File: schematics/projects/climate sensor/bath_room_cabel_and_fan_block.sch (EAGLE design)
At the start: 5 parts

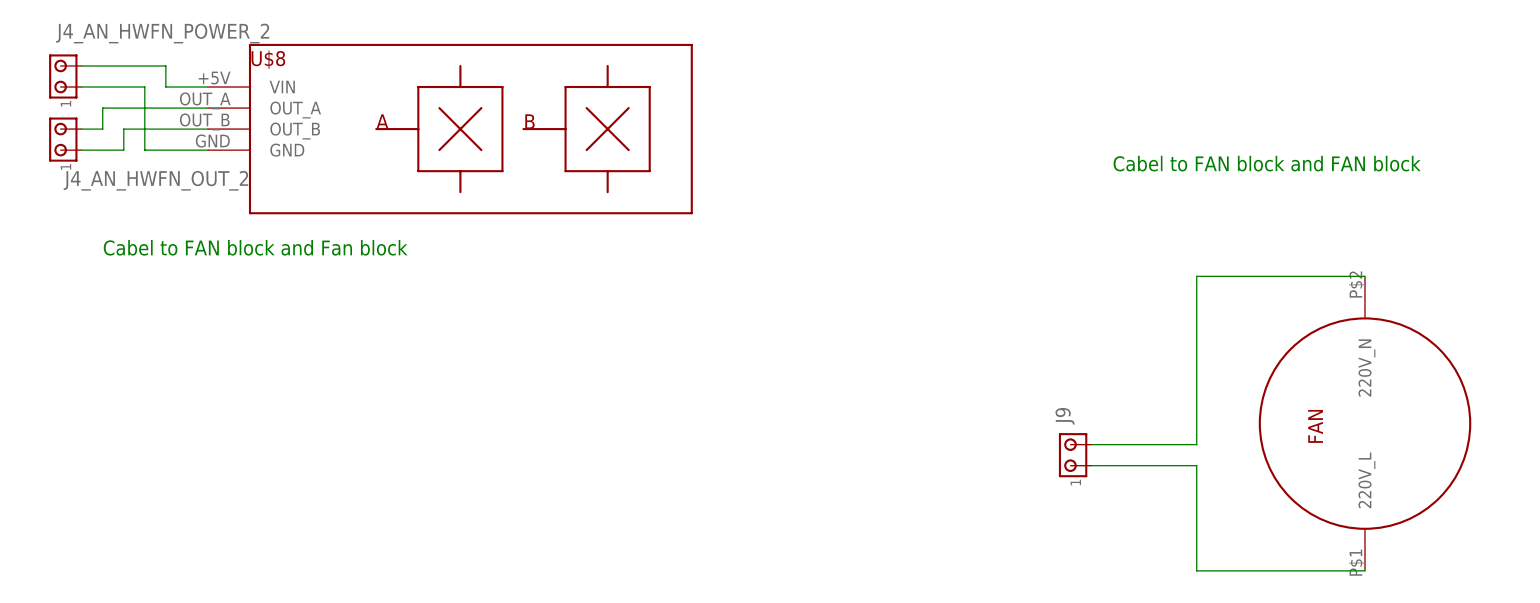
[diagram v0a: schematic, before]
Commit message: added eagle board files for low-voltage schemas
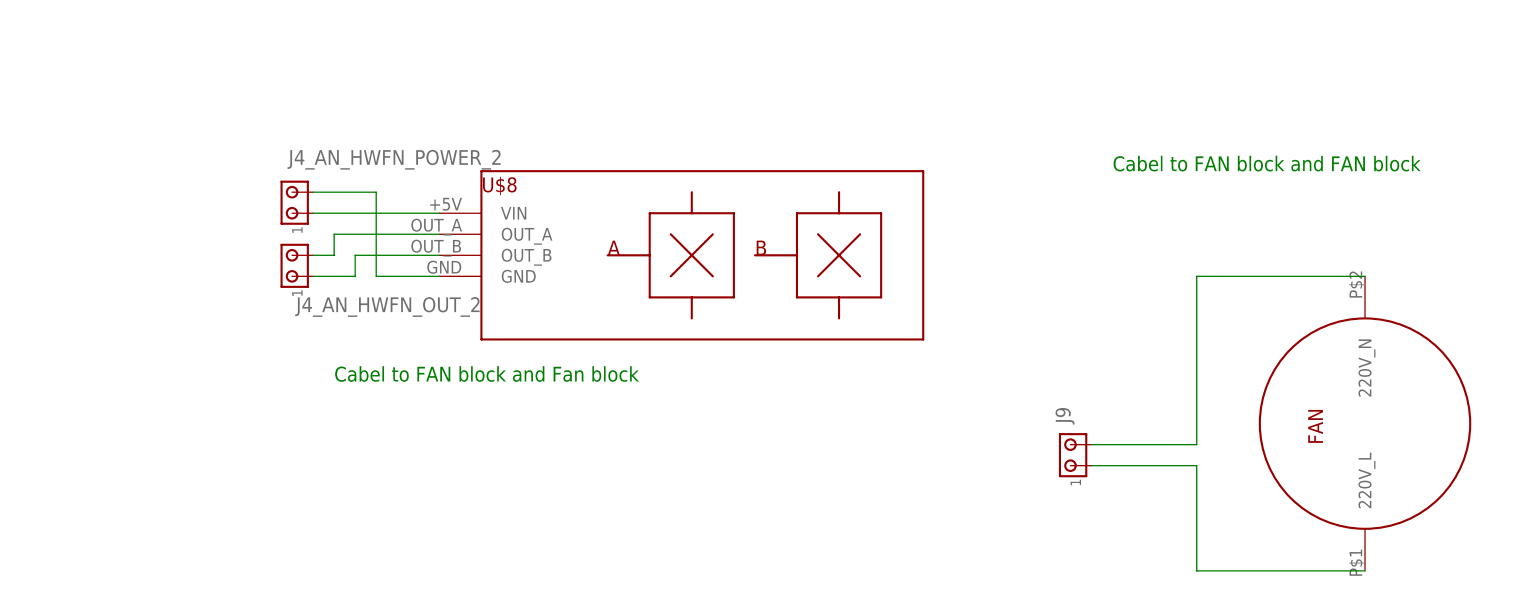
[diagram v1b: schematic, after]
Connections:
- net GND: now also J4_AN_HWFN_POWER_2.2; no longer J4_AN_HWFN_POWER_2.1
- net N$12: now also J4_AN_HWFN_POWER_2.1; no longer J4_AN_HWFN_POWER_2.2
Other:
- moved on the sheet: J4_AN_HWFN_OUT_2, J4_AN_HWFN_POWER_2, U$8
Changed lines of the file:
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@@
 </classes>
 <groups>
+<schematic_group name="FAN1"/>
 <schematic_group name="ANEMOMETER1"/>
-<schematic_group name="FAN1"/>
 </groups>
 <parts>
+<part name="U$10" library="my_devices" deviceset="FAN" device=""/>
+<part name="J9" library="con-amp" library_urn="urn:adsk.eagle:library:127" deviceset="MTA02-100" device="" package3d_urn="urn:adsk.eagle:package:8081649/1"/>
 <part name="U$8" library="my_devices" deviceset="ANEMOMETER" device=""/>
 <part name="J4_AN_HWFN_POWER_2" library="con-amp" library_urn="urn:adsk.eagle:library:127" deviceset="MTA02-100" device="" package3d_urn="urn:adsk.eagle:package:8081649/1"/>
 <part name="J4_AN_HWFN_OUT_2" library="con-amp" library_urn="urn:adsk.eagle:library:127" deviceset="MTA02-100" device="" package3d_urn="urn:adsk.eagle:package:8081649/1"/>
-<part name="U$10" library="my_devices" deviceset="FAN" device=""/>
-<part name="J9" library="con-amp" library_urn="urn:adsk.eagle:library:127" deviceset="MTA02-100" device="" package3d_urn="urn:adsk.eagle:package:8081649/1"/>
 </parts>
 <sheets>
 <sheet>
 <plain>
-<text x="-86.36" y="73.66" size="1.778" layer="91" grouprefs="ANEMOMETER1">Cabel to FAN block and Fan block</text>
 <text x="35.56" y="83.82" size="1.778" layer="91" grouprefs="FAN1">Cabel to FAN block and FAN block</text>
+<text x="-58.42" y="58.42" size="1.778" layer="91" grouprefs="ANEMOMETER1">Cabel to FAN block and Fan block</text>
 </plain>
 <instances>
-<instance part="U$8" gate="G$1" x="-53.34" y="88.9" smashed="yes" grouprefs="ANEMOMETER1">
-<attribute name="NAME" x="-68.58" y="96.52" size="1.778" layer="94"/>
-</instance>
-<instance part="J4_AN_HWFN_POWER_2" gate="G$1" x="-91.44" y="93.98" smashed="yes" rot="R90" grouprefs="ANEMOMETER1">
-<attribute name="NAME" x="-66.04" y="101.6" size="1.778" layer="95" rot="R180"/>
-<attribute name="VALUE" x="-87.63" y="99.06" size="1.778" layer="96" rot="R90"/>
-</instance>
-<instance part="J4_AN_HWFN_OUT_2" gate="G$1" x="-91.44" y="86.36" smashed="yes" rot="R90" grouprefs="ANEMOMETER1">
-<attribute name="NAME" x="-68.58" y="83.82" size="1.778" layer="95" rot="R180"/>
-<attribute name="VALUE" x="-87.63" y="91.44" size="1.778" layer="96" rot="R90"/>
-</instance>
 <instance part="U$10" gate="G$1" x="66.04" y="53.34" smashed="yes" rot="R90" grouprefs="FAN1"/>
 <instance part="J9" gate="G$1" x="30.48" y="48.26" smashed="yes" rot="R90" grouprefs="FAN1">
@@
 <attribute name="VALUE" x="34.29" y="53.34" size="1.778" layer="96" rot="R90"/>
 </instance>
+<instance part="U$8" gate="G$1" x="-25.4" y="73.66" smashed="yes" grouprefs="ANEMOMETER1">
+<attribute name="NAME" x="-40.64" y="81.28" size="1.778" layer="94"/>
+</instance>
+<instance part="J4_AN_HWFN_POWER_2" gate="G$1" x="-63.5" y="78.74" smashed="yes" rot="R90" grouprefs="ANEMOMETER1">
+<attribute name="NAME" x="-38.1" y="86.36" size="1.778" layer="95" rot="R180"/>
+<attribute name="VALUE" x="-59.69" y="83.82" size="1.778" layer="96" rot="R90"/>
+</instance>
+<instance part="J4_AN_HWFN_OUT_2" gate="G$1" x="-63.5" y="71.12" smashed="yes" rot="R90" grouprefs="ANEMOMETER1">
+<attribute name="NAME" x="-40.64" y="68.58" size="1.778" layer="95" rot="R180"/>
+<attribute name="VALUE" x="-59.69" y="76.2" size="1.778" layer="96" rot="R90"/>
+</instance>
 </instances>
 <busses>
 </busses>
 <nets>
-<net name="GND" class="0">
-<segment>
-<pinref part="U$8" gate="G$1" pin="GND"/>
-<wire x1="-73.66" y1="86.36" x2="-81.28" y2="86.36" width="0.1524" layer="91" grouprefs="ANEMOMETER1"/>
-<wire x1="-81.28" y1="86.36" x2="-81.28" y2="93.98" width="0.1524" layer="91" grouprefs="ANEMOMETER1"/>
-<pinref part="J4_AN_HWFN_POWER_2" gate="G$1" pin="1"/>
-<wire x1="-81.28" y1="93.98" x2="-88.9" y2="93.98" width="0.1524" layer="91" grouprefs="ANEMOMETER1"/>
-</segment>
-</net>
-<net name="N$12" class="0">
-<segment>
-<pinref part="U$8" gate="G$1" pin="VIN"/>
-<wire x1="-73.66" y1="93.98" x2="-78.74" y2="93.98" width="0.1524" layer="91" grouprefs="ANEMOMETER1"/>
-<wire x1="-78.74" y1="93.98" x2="-78.74" y2="96.52" width="0.1524" layer="91" grouprefs="ANEMOMETER1"/>
-<pinref part="J4_AN_HWFN_POWER_2" gate="G$1" pin="2"/>
-<wire x1="-78.74" y1="96.52" x2="-88.9" y2="96.52" width="0.1524" layer="91" grouprefs="ANEMOMETER1"/>
-</segment>
-</net>
-<net name="N$13" class="0">
-<segment>
-<pinref part="U$8" gate="G$1" pin="OUT_A"/>
-<wire x1="-73.66" y1="91.44" x2="-86.36" y2="91.44" width="0.1524" layer="91" grouprefs="ANEMOMETER1"/>
-<wire x1="-86.36" y1="91.44" x2="-86.36" y2="88.9" width="0.1524" layer="91" grouprefs="ANEMOMETER1"/>
-<pinref part="J4_AN_HWFN_OUT_2" gate="G$1" pin="2"/>
-<wire x1="-86.36" y1="88.9" x2="-88.9" y2="88.9" width="0.1524" layer="91" grouprefs="ANEMOMETER1"/>
-</segment>
-</net>
-<net name="N$14" class="0">
-<segment>
-<pinref part="U$8" gate="G$1" pin="OUT_B"/>
-<wire x1="-73.66" y1="88.9" x2="-83.82" y2="88.9" width="0.1524" layer="91" grouprefs="ANEMOMETER1"/>
-<wire x1="-83.82" y1="88.9" x2="-83.82" y2="86.36" width="0.1524" layer="91" grouprefs="ANEMOMETER1"/>
-<pinref part="J4_AN_HWFN_OUT_2" gate="G$1" pin="1"/>
-<wire x1="-83.82" y1="86.36" x2="-88.9" y2="86.36" width="0.1524" layer="91" grouprefs="ANEMOMETER1"/>
-</segment>
-</net>
 <net name="N$15" class="0">
 <segment>
@@
 </segment>
 </net>
+<net name="GND" class="0">
+<segment>
+<pinref part="J4_AN_HWFN_POWER_2" gate="G$1" pin="2"/>
+<wire x1="-60.96" y1="81.28" x2="-53.34" y2="81.28" width="0.1524" layer="91" grouprefs="ANEMOMETER1"/>
+<wire x1="-53.34" y1="81.28" x2="-53.34" y2="71.12" width="0.1524" layer="91" grouprefs="ANEMOMETER1"/>
+<pinref part="U$8" gate="G$1" pin="GND"/>
+<wire x1="-53.34" y1="71.12" x2="-45.72" y2="71.12" width="0.1524" layer="91" grouprefs="ANEMOMETER1"/>
+</segment>
+</net>
+<net name="N$13" class="0">
+<segment>
+<pinref part="U$8" gate="G$1" pin="OUT_A"/>
+<wire x1="-45.72" y1="76.2" x2="-58.42" y2="76.2" width="0.1524" layer="91" grouprefs="ANEMOMETER1"/>
+<wire x1="-58.42" y1="76.2" x2="-58.42" y2="73.66" width="0.1524" layer="91" grouprefs="ANEMOMETER1"/>
+<pinref part="J4_AN_HWFN_OUT_2" gate="G$1" pin="2"/>
+<wire x1="-58.42" y1="73.66" x2="-60.96" y2="73.66" width="0.1524" layer="91" grouprefs="ANEMOMETER1"/>
+</segment>
+</net>
+<net name="N$14" class="0">
+<segment>
+<pinref part="U$8" gate="G$1" pin="OUT_B"/>
+<wire x1="-45.72" y1="73.66" x2="-55.88" y2="73.66" width="0.1524" layer="91" grouprefs="ANEMOMETER1"/>
+<wire x1="-55.88" y1="73.66" x2="-55.88" y2="71.12" width="0.1524" layer="91" grouprefs="ANEMOMETER1"/>
+<pinref part="J4_AN_HWFN_OUT_2" gate="G$1" pin="1"/>
+<wire x1="-55.88" y1="71.12" x2="-60.96" y2="71.12" width="0.1524" layer="91" grouprefs="ANEMOMETER1"/>
+</segment>
+</net>
+<net name="N$12" class="0">
+<segment>
+<pinref part="J4_AN_HWFN_POWER_2" gate="G$1" pin="1"/>
+<pinref part="U$8" gate="G$1" pin="VIN"/>
+<wire x1="-60.96" y1="78.74" x2="-45.72" y2="78.74" width="0.1524" layer="91" grouprefs="ANEMOMETER1"/>
+</segment>
+</net>
